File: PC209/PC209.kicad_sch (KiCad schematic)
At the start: 4 parts, among them J1 PC209_BoardEdge_44pin

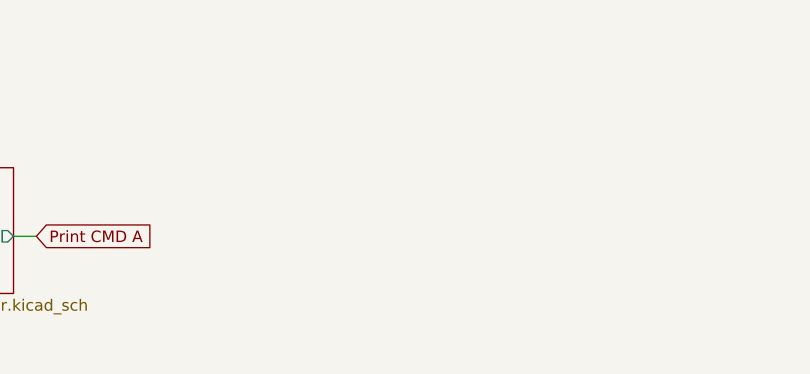
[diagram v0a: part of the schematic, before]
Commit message: PC209: Initial layout for pulse generator sections
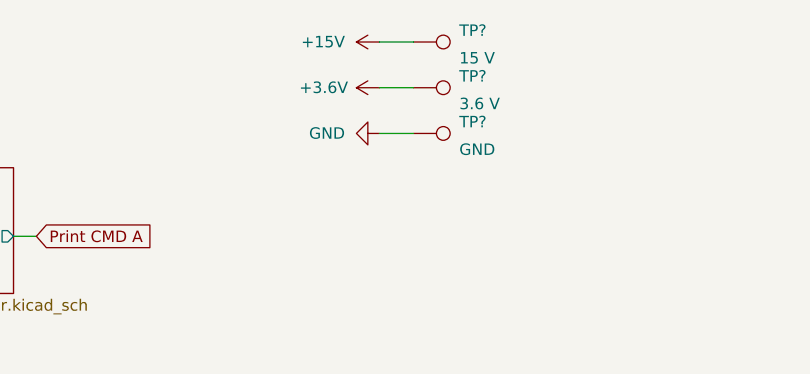
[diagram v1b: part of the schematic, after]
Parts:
- added TP?: 15 V, TestPoint:TestPoint_THTPad_2.0x2.0mm_Drill1.0mm, symbol Connector:TestPoint
- added TP?: GND, TestPoint:TestPoint_THTPad_2.0x2.0mm_Drill1.0mm, symbol Connector:TestPoint
- added TP?: 3.6 V, TestPoint:TestPoint_THTPad_2.0x2.0mm_Drill1.0mm, symbol Connector:TestPoint
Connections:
- net +15V: now also TP?.1
- net +3.6V: now also TP?.1
- net GND: now also TP?.1
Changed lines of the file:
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@@
+    (stroke (width 0) (type default) (color 0 0 0 0))
+  )
+  (wire (pts (xy 134.62 27.94) (xy 138.43 27.94))
     (stroke (width 0) (type default) (color 0 0 0 0))
   )
@@
     (stroke (width 0) (type default) (color 0 0 0 0))
   )
+  (wire (pts (xy 134.62 17.78) (xy 138.43 17.78))
+    (stroke (width 0) (type default) (color 0 0 0 0))
+  )
   (wire (pts (xy 19.05 68.58) (xy 19.05 71.12))
     (stroke (width 0) (type default) (color 0 0 0 0))
@@
   )
   (wire (pts (xy 254 38.1) (xy 256.54 38.1))
+    (stroke (width 0) (type default) (color 0 0 0 0))
+  )
+  (wire (pts (xy 134.62 22.86) (xy 138.43 22.86))
     (stroke (width 0) (type default) (color 0 0 0 0))
   )
@@
       (effects (font (size 1.27 1.27)) (justify left) hide)
     )
+  )
+  (symbol (lib_id "power:GND") (at 134.62 27.94 270) (unit 1)
+    (in_bom yes) (on_board yes) (fields_autoplaced)
+    (property "Reference" "#PWR?" (id 0) (at 128.27 27.94 0)
+      (effects (font (size 1.27 1.27)) hide)
+    )
+    (property "Value" "GND" (id 1) (at 130.81 27.9399 90)
+      (effects (font (size 1.27 1.27)) (justify right))
+    )
+    (property "Footprint" "" (id 2) (at 134.62 27.94 0)
+      (effects (font (size 1.27 1.27)) hide)
+    )
+    (property "Datasheet" "" (id 3) (at 134.62 27.94 0)
+      (effects (font (size 1.27 1.27)) hide)
+    )
+    (pin "1")
   )
   (symbol (lib_id "lib_symbols:PC209_BoardEdge_44pin") (at 233.68 20.32 0) (unit 1)
@@
     (pin "1")
   )
+  (symbol (lib_id "power:+15V") (at 134.62 17.78 90) (unit 1)
+    (in_bom yes) (on_board yes) (fields_autoplaced)
+    (property "Reference" "#PWR?" (id 0) (at 138.43 17.78 0)
+      (effects (font (size 1.27 1.27)) hide)
+    )
+    (property "Value" "+15V" (id 1) (at 130.81 17.7799 90)
+      (effects (font (size 1.27 1.27)) (justify left))
+    )
+    (property "Footprint" "" (id 2) (at 134.62 17.78 0)
+      (effects (font (size 1.27 1.27)) hide)
+    )
+    (property "Datasheet" "" (id 3) (at 134.62 17.78 0)
+      (effects (font (size 1.27 1.27)) hide)
+    )
+    (pin "1")
+  )
   (symbol (lib_id "power:GND") (at 209.55 22.86 270) (unit 1)
     (in_bom yes) (on_board yes) (fields_autoplaced)
@@
     )
     (property "Datasheet" "" (id 3) (at 209.55 22.86 0)
+      (effects (font (size 1.27 1.27)) hide)
+    )
+    (pin "1")
+  )
+  (symbol (lib_id "Connector:TestPoint") (at 138.43 17.78 270) (unit 1)
+    (in_bom no) (on_board yes)
+    (property "Reference" "TP?" (id 0) (at 143.51 16.51 90)
+      (effects (font (size 1.27 1.27)) (justify left))
+    )
+    (property "Value" "15 V" (id 1) (at 143.51 20.32 90)
+      (effects (font (size 1.27 1.27)) (justify left bottom))
+    )
+    (property "Footprint" "TestPoint:TestPoint_THTPad_2.0x2.0mm_Drill1.0mm" (id 2) (at 138.43 22.86 0)
+      (effects (font (size 1.27 1.27)) hide)
+    )
+    (property "Datasheet" "~" (id 3) (at 138.43 22.86 0)
       (effects (font (size 1.27 1.27)) hide)
     )
@@
     (pin "1")
   )
+  (symbol (lib_id "Connector:TestPoint") (at 138.43 27.94 270) (unit 1)
+    (in_bom no) (on_board yes)
+    (property "Reference" "TP?" (id 0) (at 143.51 26.67 90)
+      (effects (font (size 1.27 1.27)) (justify left))
+    )
+    (property "Value" "GND" (id 1) (at 143.51 30.48 90)
+      (effects (font (size 1.27 1.27)) (justify left bottom))
+    )
+    (property "Footprint" "TestPoint:TestPoint_THTPad_2.0x2.0mm_Drill1.0mm" (id 2) (at 138.43 33.02 0)
+      (effects (font (size 1.27 1.27)) hide)
+    )
+    (property "Datasheet" "~" (id 3) (at 138.43 33.02 0)
+      (effects (font (size 1.27 1.27)) hide)
+    )
+    (pin "1")
+  )
   (symbol (lib_id "Device:R") (at 19.05 54.61 0) (unit 1)
     (in_bom yes) (on_board yes) (fields_autoplaced)
@@
     (pin "2")
   )
+  (symbol (lib_id "Connector:TestPoint") (at 138.43 22.86 270) (unit 1)
+    (in_bom no) (on_board yes)
+    (property "Reference" "TP?" (id 0) (at 143.51 21.59 90)
+      (effects (font (size 1.27 1.27)) (justify left))
+    )
+    (property "Value" "3.6 V" (id 1) (at 143.51 25.4 90)
+      (effects (font (size 1.27 1.27)) (justify left bottom))
+    )
+    (property "Footprint" "TestPoint:TestPoint_THTPad_2.0x2.0mm_Drill1.0mm" (id 2) (at 138.43 27.94 0)
+      (effects (font (size 1.27 1.27)) hide)
+    )
+    (property "Datasheet" "~" (id 3) (at 138.43 27.94 0)
+      (effects (font (size 1.27 1.27)) hide)
+    )
+    (pin "1")
+  )
   (symbol (lib_id "power:-15V") (at 256.54 22.86 270) (unit 1)
     (in_bom yes) (on_board yes) (fields_autoplaced)
@@
     (pin "1")
     (pin "2")
+  )
+  (symbol (lib_id "lib_symbols:+3.6V") (at 134.62 22.86 90) (unit 1)
+    (in_bom yes) (on_board yes)
+    (property "Reference" "#PWR?" (id 0) (at 138.43 22.86 0)
+      (effects (font (size 1.27 1.27)) hide)
+    )
+    (property "Value" "+3.6V" (id 1) (at 125.73 22.86 90)
+      (effects (font (size 1.27 1.27)) (justify right))
+    )
+    (property "Footprint" "" (id 2) (at 134.62 22.86 0)
+      (effects (font (size 1.27 1.27)) hide)
+    )
+    (property "Datasheet" "" (id 3) (at 134.62 22.86 0)
+      (effects (font (size 1.27 1.27)) hide)
+    )
+    (pin "1")
   )
   (symbol (lib_id "lib_symbols:+3.6V") (at 85.09 24.13 0) (unit 1)
@@
       (reference "#PWR0124") (unit 1) (value "+3.6V") (footprint "")
     )
+    (path "/0bc1e519-ef4e-43a6-8cf7-e3c9063e4589"
+      (reference "#PWR?") (unit 1) (value "GND") (footprint "")
+    )
+    (path "/5536e9b0-197e-403e-854d-4a72f5c6f514"
+      (reference "#PWR?") (unit 1) (value "+15V") (footprint "")
+    )
+    (path "/c0b8a97c-7af8-4756-beda-c4fe7606dc17"
+      (reference "#PWR?") (unit 1) (value "+3.6V") (footprint "")
+    )
     (path "/6c91cec8-d836-41c3-9f96-dd4f81dc9fe7/de53374c-82c4-4235-83b9-10af35f6f0f7"
       (reference "C1") (unit 1) (value "1 nF") (footprint "Capacitor_SMD:C_0603_1608Metric")
@@
     )
     (path "/6c91cec8-d836-41c3-9f96-dd4f81dc9fe7/737ba571-9edf-4e29-937c-9e4936917a8d"
-      (reference "TP1") (unit 1) (value "Sample") (footprint "TestPoint:TestPoint_Keystone_5015_Micro-Minature")
+      (reference "TP1") (unit 1) (value "Sample") (footprint "TestPoint:TestPoint_THTPad_2.0x2.0mm_Drill1.0mm")
     )
     (path "/6c91cec8-d836-41c3-9f96-dd4f81dc9fe7/ff83114b-2617-41d3-8cbb-911623272170"
-      (reference "TP2") (unit 1) (value "10 us delay") (footprint "TestPoint:TestPoint_Keystone_5015_Micro-Minature")
+      (reference "TP2") (unit 1) (value "10 μs delay") (footprint "TestPoint:TestPoint_THTPad_2.0x2.0mm_Drill1.0mm")
     )
     (path "/6c91cec8-d836-41c3-9f96-dd4f81dc9fe7/c83aeeee-af08-4aea-9d0c-0a8f2812a98c"
-      (reference "TP3") (unit 1) (value "~Sample") (footprint "TestPoint:TestPoint_Keystone_5015_Micro-Minature")
+      (reference "TP3") (unit 1) (value "~Sample") (footprint "TestPoint:TestPoint_THTPad_2.0x2.0mm_Drill1.0mm")
     )
     (path "/6c91cec8-d836-41c3-9f96-dd4f81dc9fe7/7465aab8-a1b7-4ee6-8a4b-c683d8a1c19f"
-      (reference "TP4") (unit 1) (value "10 us delay") (footprint "TestPoint:TestPoint_Keystone_5015_Micro-Minature")
-    )
-  )
+      (reference "TP4") (unit 1) (value "100 μs pulse") (footprint "TestPoint:TestPoint_THTPad_2.0x2.0mm_Drill1.0mm")
+    )
+    (path "/6172b9a0-2c4f-46a6-9a81-086f9421cc60"
+      (reference "TP?") (unit 1) (value "15 V") (footprint "TestPoint:TestPoint_THTPad_2.0x2.0mm_Drill1.0mm")
+    )
+    (path "/72d430ef-dbeb-4e28-b6ef-ecafd51103df"
+      (reference "TP?") (unit 1) (value "GND") (footprint "TestPoint:TestPoint_THTPad_2.0x2.0mm_Drill1.0mm")
+    )
+    (path "/9d827eef-28b1-432f-9f98-ce802d55d331"
+      (reference "TP?") (unit 1) (value "3.6 V") (footprint "TestPoint:TestPoint_THTPad_2.0x2.0mm_Drill1.0mm")
+    )
+  )

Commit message: PC209: Initial board routing
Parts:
- added C7: 100 pF, Capacitor_SMD:C_0603_1608Metric, symbol Device:C_Small
- added Q10, Q11, Q12, Q13, Q14, Q15, Q16, Q17, Q8, Q9: BC848W, Package_TO_SOT_SMD:SOT-323_SC-70, symbol Transistor_BJT:BC848W
- added R20, R21, R22, R23, R24, R30, R32, R33, R35, R39: 120k, Resistor_SMD:R_0603_1608Metric, symbol Device:R_Small
- added R25, R26, R27, R28, R29, R31, R36, R37, R38: 180k, Resistor_SMD:R_0603_1608Metric, symbol Device:R_Small
- added R34: 1k, Resistor_SMD:R_0603_1608Metric, symbol Device:R_Small
- added R40, R41, R42, R43, R44, R45: 0, Resistor_SMD:R_0603_1608Metric, symbol Device:R_Small
- added U1, U2: 4010, symbol 4xxx:4010
- gave numbers to parts that had none: 3
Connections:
- net +15V: now also R25.2, R26.2, R27.2, R28.2, R29.2, R31.2, R36.2, R37.1, R38.2, U1.1 (VCC), U1.16 (VDD), U2.1 (VCC), U2.16 (VDD)
- net 1e-2 Range: now also R43.2; no longer J1.7 (Range_1e-2_Out)
- net GND: now also Q10.2 (E), Q11.2 (E), Q12.2 (E), Q13.2 (E), Q14.2 (E), Q15.2 (E), Q16.2 (E), Q17.2 (E), Q8.2 (E), Q9.2 (E), R34.1, U1.8 (VSS), U2.11, U2.14, U2.8 (VSS), U2.9
- net Hold 1: now also R42.2; no longer J1.5 (Hold_1_Out)
- net Hold 2: now also R41.2; no longer J1.4 (Hold_2_Out)
- net Print CMD A: now also U2.2
- net Print CMD B: now also U2.4
- net Range 1: now also R24.1
- net Range 1 Print: now also U1.12
- net Range 10: now also R20.1
- net Range 10 Print: now also U1.2
- net Range 2: now also R23.1
- net Range 2 Print: now also U1.10
- net Range 4: now also R22.1
- net Range 4 Print: now also U1.6
- net Range 8: now also R21.1
- net Range 8 Print: now also U1.4
- net Range Hold: now also R44.2; no longer J1.8 (Range_Hold_Out)
- net Range Signal: now also R34.2, R35.1
- net Range Signal Print: now also U2.6
- net Trigger: now also R40.2; no longer J1.3 (Trigger_Out)
- net Zero Check: now also R30.1, R45.2; no longer J1.9 (Zero_Check_Out)
- net Zero Check Print: now also U1.15
- new net: Q10.1 (B), R22.2
- new net: Q10.3 (C), R27.1, U1.7
- new net: Q13.3 (C), R31.1, U1.14
- new net: Q8.3 (C), R25.1, U1.3
- new net: Q12.1 (B), R24.2
- new net: Q12.3 (C), R29.1, U1.11
- new net: C7.2, Q15.1 (B), R33.2
- new net: Q15.3 (C), R36.1, U2.3
- new net: Q13.1 (B), R30.2
- new net: Q16.3 (C), R38.1, R39.1, U2.7
- new net: Q17.1 (B), R39.2
- new net: Q14.1 (B), R32.2
- new net: Q14.3 (C), Q17.3 (C), R37.2, U2.5
- new net: Q9.1 (B), R21.2
- new net: Q11.1 (B), R23.2
- new net: Q11.3 (C), R28.1, U1.9
- new net: Q9.3 (C), R26.1, U1.5
- new net: Q16.1 (B), R35.2
- new net: Q8.1 (B), R20.2
- new net Hold 1 Out: J1.5 (Hold_1_Out), R42.1
- new net Hold 2 Out: J1.4 (Hold_2_Out), R41.1
- new net Pulse Generator/Output: C7.1, R32.1, R33.1
- new net Range 1e-2 Out: J1.7 (Range_1e-2_Out), R43.1
- new net Range Hold Out: J1.8 (Range_Hold_Out), R44.1
- new net Trigger Out: J1.3 (Trigger_Out), R40.1
- new net Zero Check Out: J1.9 (Zero_Check_Out), R45.1
- no-connect marks 0 -> 3
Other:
- moved on the sheet: TP5, TP6, TP7

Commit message: PC209: Rev 1.0
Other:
- sheet Pulse Generator ports: added none; removed 15 V, 3.6 V, GND
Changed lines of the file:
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@@
   (title_block
     (title "Keithley 615 PC209 Replacement Board")
+    (date "2023-01-16")
+    (rev "1.0")
     (company "Peter Farley")
+    (comment 1 "Rev 1.0: Initial Design")
   )
   (junction (at 127 153.67) (diameter 0) (color 0 0 0 0)
@@
     (stroke (width 0) (type default) (color 0 0 0 0))
   )
-  (wire (pts (xy 83.82 45.72) (xy 83.82 48.26))
-    (stroke (width 0) (type default) (color 0 0 0 0))
-  )
-  (wire (pts (xy 82.55 27.94) (xy 82.55 31.75))
-    (stroke (width 0) (type default) (color 0 0 0 0))
-  )
   (wire (pts (xy 254 30.48) (xy 256.54 30.48))
     (stroke (width 0) (type default) (color 0 0 0 0))
@@
   )
   (wire (pts (xy 209.55 30.48) (xy 212.09 30.48))
-    (stroke (width 0) (type default) (color 0 0 0 0))
-  )
-  (wire (pts (xy 85.09 24.13) (xy 85.09 31.75))
     (stroke (width 0) (type default) (color 0 0 0 0))
   )
@@
     (pin "1")
   )
-  (symbol (lib_id "power:+15V") (at 82.55 27.94 0) (unit 1)
-    (in_bom yes) (on_board yes)
-    (property "Reference" "#PWR0108" (id 0) (at 82.55 31.75 0)
-      (effects (font (size 1.27 1.27)) hide)
-    )
-    (property "Value" "+15V" (id 1) (at 82.55 24.13 0))
-    (property "Footprint" "" (id 2) (at 82.55 27.94 0)
-      (effects (font (size 1.27 1.27)) hide)
-    )
-    (property "Datasheet" "" (id 3) (at 82.55 27.94 0)
-      (effects (font (size 1.27 1.27)) hide)
-    )
-    (pin "1")
-  )
   (symbol (lib_id "4xxx:4010") (at 58.42 170.18 0) (unit 6)
     (in_bom yes) (on_board yes) (fields_autoplaced)
@@
     (pin "1")
   )
-  (symbol (lib_id "power:GND") (at 83.82 48.26 0) (unit 1)
-    (in_bom yes) (on_board yes)
-    (property "Reference" "#PWR0107" (id 0) (at 83.82 54.61 0)
-      (effects (font (size 1.27 1.27)) hide)
-    )
-    (property "Value" "GND" (id 1) (at 83.82 52.07 0))
-    (property "Footprint" "" (id 2) (at 83.82 48.26 0)
-      (effects (font (size 1.27 1.27)) hide)
-    )
-    (property "Datasheet" "" (id 3) (at 83.82 48.26 0)
-      (effects (font (size 1.27 1.27)) hide)
-    )
-    (pin "1")
-  )
   (symbol (lib_id "power:+15V") (at 36.83 170.18 90) (unit 1)
     (in_bom yes) (on_board yes)
@@
     (pin "1")
   )
-  (symbol (lib_id "lib_symbols:+3.6V") (at 85.09 24.13 0) (unit 1)
-    (in_bom yes) (on_board yes) (fields_autoplaced)
-    (property "Reference" "#PWR0109" (id 0) (at 85.09 27.94 0)
-      (effects (font (size 1.27 1.27)) hide)
-    )
-    (property "Value" "+3.6V" (id 1) (at 85.09 19.05 0))
-    (property "Footprint" "" (id 2) (at 85.09 24.13 0)
-      (effects (font (size 1.27 1.27)) hide)
-    )
-    (property "Datasheet" "" (id 3) (at 85.09 24.13 0)
-      (effects (font (size 1.27 1.27)) hide)
-    )
-    (pin "1")
-  )
   (symbol (lib_id "Transistor_BJT:BC848W") (at 125.73 96.52 0) (unit 1)
     (in_bom yes) (on_board yes) (fields_autoplaced)
@@
       (effects (font (size 1.27 1.27)) (justify left top))
     )
-    (pin "GND" input (at 83.82 45.72 270)
-      (effects (font (size 1.27 1.27)) (justify left))
-    )
-    (pin "15 V" input (at 82.55 31.75 90)
-      (effects (font (size 1.27 1.27)) (justify right))
-    )
     (pin "Output" output (at 93.98 39.37 0)
       (effects (font (size 1.27 1.27)) (justify right))
@@
     (pin "Input" input (at 74.93 39.37 180)
       (effects (font (size 1.27 1.27)) (justify left))
-    )
-    (pin "3.6 V" input (at 85.09 31.75 90)
-      (effects (font (size 1.27 1.27)) (justify right))
     )
   )
@@
       (reference "#PWR0106") (unit 1) (value "+15V") (footprint "")
     )
-    (path "/81b6eb87-b6fb-4ab8-9d69-e9a6c99984b4"
-      (reference "#PWR0107") (unit 1) (value "GND") (footprint "")
-    )
-    (path "/630b709e-9812-457c-bc1d-76a6e1bc5fa3"
-      (reference "#PWR0108") (unit 1) (value "+15V") (footprint "")
-    )
-    (path "/e887026c-d1d8-4c75-811f-25246dddf590"
-      (reference "#PWR0109") (unit 1) (value "+3.6V") (footprint "")
-    )
     (path "/6c91cec8-d836-41c3-9f96-dd4f81dc9fe7/e08edcee-4611-4e87-a2e3-ccffe62055bf"
       (reference "#PWR0110") (unit 1) (value "+3.6V") (footprint "")
@@
       (reference "#PWR0116") (unit 1) (value "GND") (footprint "")
     )
-    (path "/6c91cec8-d836-41c3-9f96-dd4f81dc9fe7/15f003b9-c748-45cc-b282-e6c204e242f8"
-      (reference "#PWR0117") (unit 1) (value "+15V") (footprint "")
-    )
-    (path "/6c91cec8-d836-41c3-9f96-dd4f81dc9fe7/0f7b72f3-01e9-479a-9125-b281de7d6d1e"
-      (reference "#PWR0118") (unit 1) (value "+3.6V") (footprint "")
-    )
-    (path "/6c91cec8-d836-41c3-9f96-dd4f81dc9fe7/80e1d1d1-c839-4f49-861f-0bd2e114f458"
-      (reference "#PWR0119") (unit 1) (value "GND") (footprint "")
-    )
     (path "/6c91cec8-d836-41c3-9f96-dd4f81dc9fe7/7aa9f52d-f4a1-483c-9f7e-63bd2e9298d3"

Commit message: PC209: Fix silkscreen error, backannotate to schematic.
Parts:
- U1, U2: footprint (none) -> Package_SO:SOIC-16_3.9x9.9mm_P1.27mm
- renumbered C7 to C2, Q16 to Q1, Q17 to Q16, Q14 to Q17, Q12 to Q3, Q11 to Q4, Q10 to Q5, Q9 to Q6, Q8 to Q7, Q13 to Q8, Q15 to Q9, R38 to R1, R35 to R10, R24 to R12, R23 to R13, R22 to R14, R21 to R15, R20 to R16, R30 to R17, R33 to R18, R36 to R19, R29 to R3, R39 to R31, R37 to R32, R32 to R35, R40 to R36, R41 to R37, R42 to R38, R43 to R39, R28 to R4, R44 to R40, R45 to R41, R1 to R42, R2 to R43, R3 to R44, R34 to R45, R27 to R5, R26 to R6, R25 to R7, R31 to R8, TP7 to TP1, TP6 to TP2, TP5 to TP3

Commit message: PC209: Fix position of -15 V and +3.6 V on card edge
Update component values
Make library path relative
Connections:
- net +3.6V: now also J1.23 (+3.6V); no longer J1.24 (+3.6V)
- net -15V: now also J1.24 (-15V); no longer J1.23 (-15V)

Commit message: PC209: Add BOM
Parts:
- C2, R36, R37, R38, R39, R40, R41, R45: Digikey (none) -> https://www.digikey.com/en/products/detail/walsin-technolog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
- Q1, Q16, Q17, Q3, Q4, Q5, Q6, Q7, Q8, Q9: Digikey (none) -> https://www.digikey.com/en/products/detail/nexperia-usa-inc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
- R1, R10, R12, R13, R14, R15, R16, R17, R18, R19, R3, R31, R32, R35, R4, R5, R6, R7, R8: Digikey (none) -> https://www.digikey.com/en/products/detail/yageo/RC0603FR-1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
- R42, R43, R44: Digikey (none) -> https://www.digikey.com/en/products/detail/yageo/RC0603FR-0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
- U1, U2: Digikey (none) -> https://www.digikey.com/en/products/detail/texas-instrument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

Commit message: DNI R31 from PC209
This resistor prevents sensitivity 2x10^0 from hitting the proper logic levels.
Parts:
- R31: now not fitted
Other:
- note added: "Populating R31 causes a low voltage into U2.7, due to the current sunk by the base of Q16. Alternatively, this could be addressed by increasing the value of R31. But Print CMD B is unused by the 615 anyway."
